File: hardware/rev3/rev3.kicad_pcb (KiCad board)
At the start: 4 copper layers, 55.9 x 76.2 mm, 109 parts, among them J1 USB_B, J2 SMA, J3 CONN_02X09, J4 SMA, J5 CONN_02X09, J6 SMA, J7 SMA, U1 LD1117S33TR, U2 93LCxxB, U3 FT2232H, U4 LTC6409, U5 LTC6269, U6 AD9102, X1 DSC1123, Y1 12MHz

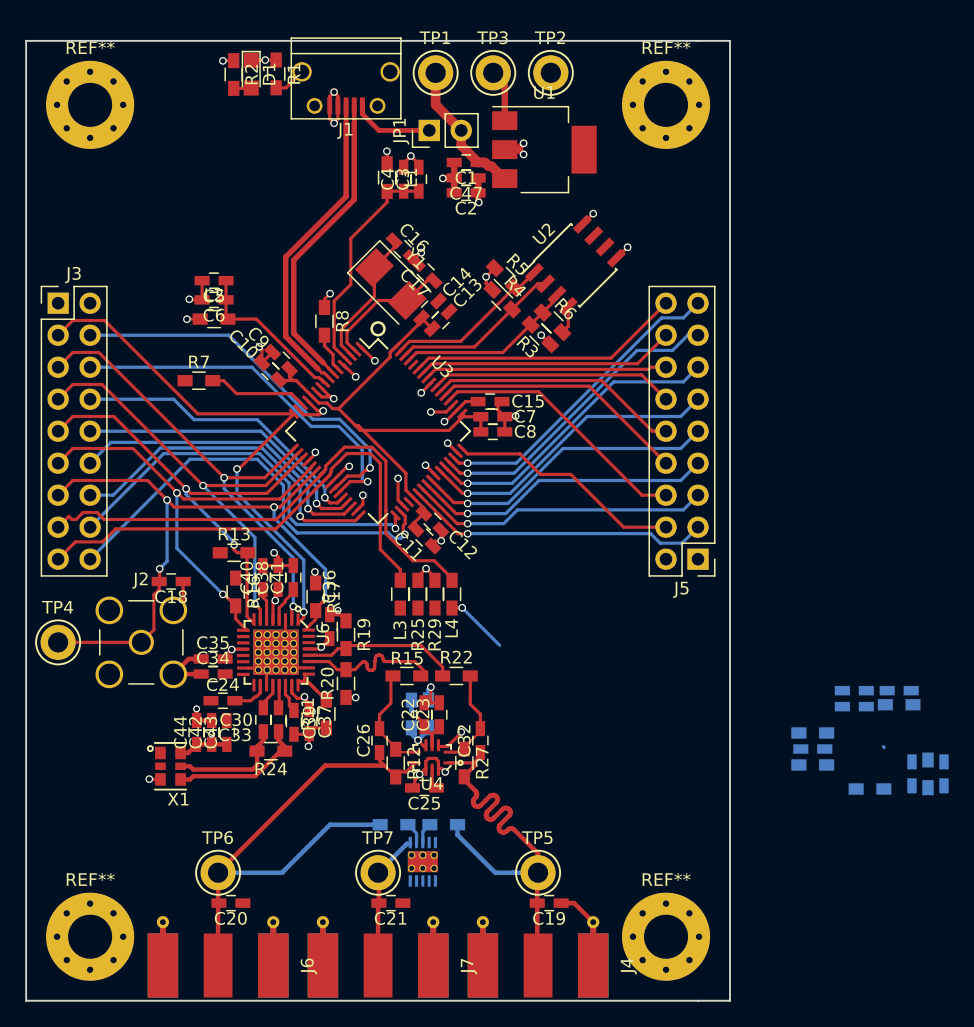
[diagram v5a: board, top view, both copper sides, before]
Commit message: Initial attempt at a complete layout.
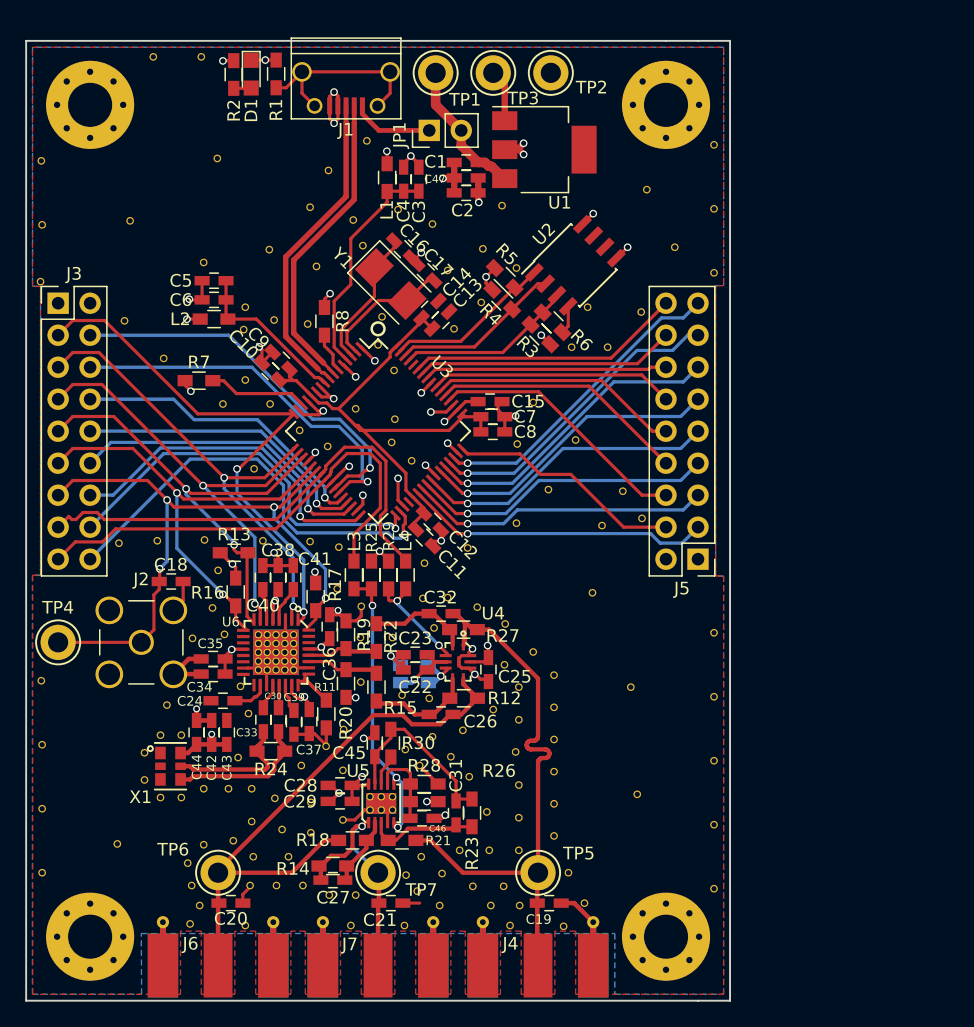
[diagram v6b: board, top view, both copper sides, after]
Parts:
- added ?: , footprints:ManualVia, F.Cu at (133.1, 85.8)
- added ?: , footprints:ManualVia, F.Cu at (141.3, 61.8)
- added ?: , footprints:ManualVia, F.Cu at (160.0, 79.3)
- added ?: , footprints:ManualVia, F.Cu at (162.2, 81.5)
- added ?: , footprints:ManualVia, F.Cu at (163.8, 83.4)
- added ?: , footprints:ManualVia, F.Cu at (163.8, 85.9)
- added ?: , footprints:ManualVia, F.Cu at (163.8, 88.5)
- added ?: , footprints:ManualVia, F.Cu at (163.8, 91.0)
- added ?: , footprints:ManualVia, F.Cu at (163.8, 93.6)
- added ?: , footprints:ManualVia, F.Cu at (163.8, 96.1)
- added ?: , footprints:ManualVia, F.Cu at (165.0, 99.1)
- added ?: , footprints:ManualVia, F.Cu at (166.2, 101.5)
- added ?: , footprints:ManualVia, F.Cu at (137.5, 61.8)
- added ?: , footprints:ManualVia, F.Cu at (164.6, 103.3)
- added ?: , footprints:ManualVia, F.Cu at (160.3, 103.3)
- added ?: , footprints:ManualVia, F.Cu at (161.1, 101.7)
- added ?: , footprints:ManualVia, F.Cu at (158.8, 101.7)
- added ?: , footprints:ManualVia, F.Cu at (154.7, 101.7)
- added ?: , footprints:ManualVia, F.Cu at (153.0, 100.5)
- added ?: , footprints:ManualVia, F.Cu at (152.1, 99.3)
- added ?: , footprints:ManualVia, F.Cu at (153.3, 97.8)
- added ?: , footprints:ManualVia, F.Cu at (154.9, 99.1)
- added ?: , footprints:ManualVia, F.Cu at (157.4, 100.1)
- added ?: , footprints:ManualVia, F.Cu at (130.2, 47.3)
- added ?: , footprints:ManualVia, F.Cu at (159.8, 100.1)
- added ?: , footprints:ManualVia, F.Cu at (135.1, 100.1)
- added ?: , footprints:ManualVia, F.Cu at (134.7, 98.3)
- added ?: , footprints:ManualVia, F.Cu at (136.0, 96.8)
- added ?: , footprints:ManualVia, F.Cu at (138.4, 96.5)
- added ?: , footprints:ManualVia, F.Cu at (139.8, 95.0)
- added ?: , footprints:ManualVia, F.Cu at (141.7, 93.2)
- added ?: , footprints:ManualVia, F.Cu at (148.5, 83.9)
- added ?: , footprints:ManualVia, F.Cu at (147.1, 87.7)
- added ?: , footprints:ManualVia, F.Cu at (145.7, 89.0)
- added ?: , footprints:ManualVia, F.Cu at (137.1, 42.4)
- added ?: , footprints:ManualVia, F.Cu at (143.8, 90.6)
- added ?: , footprints:ManualVia, F.Cu at (139.8, 92.4)
- added ?: , footprints:ManualVia, F.Cu at (138.0, 92.4)
- added ?: , footprints:ManualVia, F.Cu at (136.0, 92.4)
- added ?: , footprints:ManualVia, F.Cu at (134.2, 93.1)
- added ?: , footprints:ManualVia, F.Cu at (161.0, 92.1)
- added ?: , footprints:ManualVia, F.Cu at (161.0, 94.7)
- added ?: , footprints:ManualVia, F.Cu at (161.0, 97.3)
- added ?: , footprints:ManualVia, F.Cu at (158.7, 97.3)
- added ?: , footprints:ManualVia, F.Cu at (156.3, 97.3)
- added ?: , footprints:ManualVia, F.Cu at (158.2, 49.5)
- added ?: , footprints:ManualVia, F.Cu at (158.5, 94.2)
- added ?: , footprints:ManualVia, F.Cu at (157.1, 91.4)
- added ?: , footprints:ManualVia, F.Cu at (154.2, 88.3)
- added ?: , footprints:ManualVia, F.Cu at (156.6, 87.8)
- added ?: , footprints:ManualVia, F.Cu at (155.6, 89.9)
- added ?: , footprints:ManualVia, F.Cu at (153.2, 90.6)
- added ?: , footprints:ManualVia, F.Cu at (152.0, 89.3)
- added ?: , footprints:ManualVia, F.Cu at (161.0, 84.3)
- added ?: , footprints:ManualVia, F.Cu at (161.0, 86.9)
- added ?: , footprints:ManualVia, F.Cu at (159.9, 82.5)
- added ?: , footprints:ManualVia, F.Cu at (173.4, 49.4)
- added ?: , footprints:ManualVia, F.Cu at (159.0, 86.1)
- added ?: , footprints:ManualVia, F.Cu at (160.8, 89.5)
- added ?: , footprints:ManualVia, F.Cu at (148.1, 100.8)
- added ?: , footprints:ManualVia, F.Cu at (146.0, 100.8)
- added ?: , footprints:ManualVia, F.Cu at (143.9, 100.1)
- added ?: , footprints:ManualVia, F.Cu at (141.8, 100.1)
- added ?: , footprints:ManualVia, F.Cu at (139.7, 100.1)
- added ?: , footprints:ManualVia, F.Cu at (132.6, 93.1)
- added ?: , footprints:ManualVia, F.Cu at (131.3, 91.7)
- added ?: , footprints:ManualVia, F.Cu at (131.3, 89.5)
- added ?: , footprints:ManualVia, F.Cu at (171.2, 44.8)
- added ?: , footprints:ManualVia, F.Cu at (132.6, 88.1)
- added ?: , footprints:ManualVia, F.Cu at (134.2, 88.1)
- added ?: , footprints:ManualVia, F.Cu at (154.3, 79.6)
- added ?: , footprints:ManualVia, F.Cu at (151.0, 80.4)
- added ?: , footprints:ManualVia, F.Cu at (151.8, 85.0)
- added ?: , footprints:ManualVia, F.Cu at (153.9, 85.2)
- added ?: , footprints:ManualVia, F.Cu at (147.1, 94.9)
- added ?: , footprints:ManualVia, F.Cu at (144.5, 95.9)
- added ?: , footprints:ManualVia, F.Cu at (142.7, 97.8)
- added ?: , footprints:ManualVia, F.Cu at (144.5, 93.5)
- added ?: , footprints:ManualVia, F.Cu at (159.7, 46.1)
- added ?: , footprints:ManualVia, F.Cu at (142.2, 95.6)
- added ?: , footprints:ManualVia, F.Cu at (140.0, 97.8)
- added ?: , footprints:ManualVia, F.Cu at (147.1, 90.9)
- added ?: , footprints:ManualVia, F.Cu at (154.2, 47.6)
- added ?: , footprints:ManualVia, F.Cu at (155.4, 51.2)
- added ?: , footprints:ManualVia, F.Cu at (138.9, 84.3)
- added ?: , footprints:ManualVia, F.Cu at (149.9, 57.1)
- added ?: , footprints:ManualVia, F.Cu at (150.2, 54.9)
- added ?: , footprints:ManualVia, F.Cu at (160.8, 51.1)
- added ?: , footprints:ManualVia, F.Cu at (155.9, 55.9)
- added ?: , footprints:ManualVia, F.Cu at (158.1, 53.8)
- added ?: , footprints:ManualVia, F.Cu at (151.4, 46.4)
- added ?: , footprints:ManualVia, F.Cu at (148.7, 49.3)
- added ?: , footprints:ManualVia, F.Cu at (145.9, 43.3)
- added ?: , footprints:ManualVia, F.Cu at (144.5, 46.2)
- added ?: , footprints:ManualVia, F.Cu at (176.5, 51.4)
- added ?: , footprints:ManualVia, F.Cu at (144.3, 55.5)
- added ?: , footprints:ManualVia, F.Cu at (176.5, 41.3)
- added ?: , footprints:ManualVia, F.Cu at (176.5, 46.4)
- added ?: , footprints:ManualVia, F.Cu at (132.0, 34.3)
- added ?: , footprints:ManualVia, F.Cu at (135.8, 34.3)
- added ?: , footprints:ManualVia, F.Cu at (123.1, 42.5)
- added ?: , footprints:ManualVia, F.Cu at (123.2, 47.6)
- added ?: , footprints:ManualVia, F.Cu at (123.1, 52.1)
- added ?: , footprints:ManualVia, F.Cu at (139.3, 54.2)
- added ?: , footprints:ManualVia, F.Cu at (141.2, 49.6)
- added ?: , footprints:ManualVia, F.Cu at (141.6, 55.2)
- added ?: , footprints:ManualVia, F.Cu at (139.6, 86.4)
- added ?: , footprints:ManualVia, F.Cu at (136.0, 50.6)
- added ?: , footprints:ManualVia, F.Cu at (129.7, 55.2)
- added ?: , footprints:ManualVia, F.Cu at (139.2, 55.9)
- added ?: , footprints:ManualVia, F.Cu at (132.8, 58.2)
- added ?: , footprints:ManualVia, F.Cu at (139.3, 59.9)
- added ?: , footprints:ManualVia, F.Cu at (140.0, 67.0)
- added ?: , footprints:ManualVia, F.Cu at (145.9, 65.2)
- added ?: , footprints:ManualVia, F.Cu at (143.6, 63.9)
- added ?: , footprints:ManualVia, F.Cu at (151.2, 63.1)
- added ?: , footprints:ManualVia, F.Cu at (151.1, 59.2)
- added ?: , footprints:ManualVia, F.Cu at (138.7, 89.9)
- added ?: , footprints:ManualVia, F.Cu at (148.1, 62.2)
- added ?: , footprints:ManualVia, F.Cu at (152.5, 66.4)
- added ?: , footprints:ManualVia, F.Cu at (150.9, 64.9)
- added ?: , footprints:ManualVia, F.Cu at (169.9, 84.3)
- added ?: , footprints:ManualVia, F.Cu at (170.4, 92.8)
- added ?: , footprints:ManualVia, F.Cu at (166.9, 76.8)
- added ?: , footprints:ManualVia, F.Cu at (167.6, 71.5)
- added ?: , footprints:ManualVia, F.Cu at (163.4, 68.6)
- added ?: , footprints:ManualVia, F.Cu at (160.8, 71.3)
- added ?: , footprints:ManualVia, F.Cu at (157.0, 73.3)
- added ?: , footprints:ManualVia, F.Cu at (145.0, 50.9)
- added ?: , footprints:ManualVia, F.Cu at (153.5, 74.5)
- added ?: , footprints:ManualVia, F.Cu at (170.8, 54.5)
- added ?: , footprints:ManualVia, F.Cu at (166.5, 54.2)
- added ?: , footprints:ManualVia, F.Cu at (168.1, 57.3)
- added ?: , footprints:ManualVia, F.Cu at (165.2, 57.3)
- added ?: , footprints:ManualVia, F.Cu at (160.9, 65.0)
- added ?: , footprints:ManualVia, F.Cu at (162.2, 61.7)
- added ?: , footprints:ManualVia, F.Cu at (165.5, 64.7)
- added ?: , footprints:ManualVia, F.Cu at (169.3, 68.8)
- added ?: , footprints:ManualVia, F.Cu at (170.8, 70.9)
- added ?: , footprints:ManualVia, F.Cu at (147.9, 47.2)
- added ?: , footprints:ManualVia, F.Cu at (176.5, 80.0)
- added ?: , footprints:ManualVia, F.Cu at (176.5, 85.1)
- added ?: , footprints:ManualVia, F.Cu at (176.5, 95.2)
- added ?: , footprints:ManualVia, F.Cu at (176.5, 100.3)
- added ?: , footprints:ManualVia, F.Cu at (176.5, 90.2)
- added ?: , footprints:ManualVia, F.Cu at (123.1, 83.8)
- added ?: , footprints:ManualVia, F.Cu at (123.2, 88.9)
- added ?: , footprints:ManualVia, F.Cu at (123.2, 94.0)
- added ?: , footprints:ManualVia, F.Cu at (123.2, 99.1)
- added ?: , footprints:ManualVia, F.Cu at (135.7, 101.7)
- added ?: , footprints:ManualVia, F.Cu at (149.0, 41.0)
- added ?: , footprints:ManualVia, F.Cu at (134.9, 103.1)
- added ?: , footprints:ManualVia, F.Cu at (139.3, 103.3)
- added ?: , footprints:ManualVia, F.Cu at (147.7, 103.3)
- added ?: , footprints:ManualVia, F.Cu at (152.0, 103.3)
- added ?: , footprints:ManualVia, F.Cu at (135.1, 80.5)
- added ?: , footprints:ManualVia, F.Cu at (136.7, 78.0)
- added ?: , footprints:ManualVia, F.Cu at (137.7, 80.1)
- added ?: , footprints:ManualVia, F.Cu at (129.3, 72.9)
- added ?: , footprints:ManualVia, F.Cu at (132.3, 72.7)
- added ?: , footprints:ManualVia, F.Cu at (137.2, 75.1)
- added ?: , footprints:ManualVia, F.Cu at (129.2, 96.8)
- added ?: , footprints:ManualVia, F.Cu at (136.1, 72.6)
- added ?: , footprints:ManualVia, F.Cu at (140.7, 72.7)
- added ?: , footprints:ManualVia, F.Cu at (144.5, 72.8)
- added ?: , footprints:ManualVia, F.Cu at (146.7, 73.2)
- added ?: , footprints:ManualVia, F.Cu at (146.6, 76.5)
- added ?: , footprints:ManualVia, F.Cu at (148.5, 77.9)
- added ?: , footprints:ManualVia, F.Cu at (148.5, 80.4)
- added ?: , footprints:ManualVia, F.Cu at (153.4, 77.3)
- added ?: , footprints:ManualVia, F.Cu at (155.4, 77.2)
- added ?: , footprints:ManualVia, F.Cu at (157.7, 78.0)
-  C19: renamed from C19
- C27, C28, C29, C31, C45, C46, R14, R18, R21, R23, R26, R28, R30, U5: moved to F.Cu
- moved C27 47.4 mm to (146.3, 99.6)
- moved R14 46.7 mm to (146.3, 98.5)
- moved C45 45.2 mm to (149.6, 88.9)
- moved C28 41.5 mm to (146.8, 92.1), turned to 180 degrees
- moved C29 41.5 mm to (146.8, 93.4), turned to 180 degrees
- moved R30 38.2 mm to (150.9, 88.8), turned to 90 degrees
- moved C31 36.3 mm to (156.0, 94.3), turned to 270 degrees
- moved R23 36.3 mm to (157.3, 94.3), turned to 90 degrees
- moved C46 31.5 mm to (153.3, 94.7), turned to 0 degrees
- moved R28 31.1 mm to (153.5, 92.0), turned to 0 degrees
- moved R26 31.0 mm to (153.5, 93.4), turned to 180 degrees
- moved C25 10.7 mm to (158.6, 82.9), turned to 270 degrees
- moved R27 10.6 mm to (156.6, 79.8), turned to 0 degrees
- moved C32 10.5 mm to (154.9, 78.5), turned to 180 degrees
- moved U4 7.87 mm to (156.2, 82.3), turned to 270 degrees
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- renumbered REF** to ?
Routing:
- net GNDA: track 88.0 -> 143.6 mm, vias 30 -> 31
- net Net-(L3-Pad1): track 0.00 -> 22.6 mm, vias 0 -> 3
- net /Analog/+1.65V: track 0.00 -> 14.7 mm
- net Net-(J1-Pad5): track 2.57 -> 15.8 mm
- net +3V3: track 43.7 -> 55.1 mm, vias 21 -> 26
- net VOUT: track 10.9 -> 19.8 mm, vias 0 -> 1
- net Net-(C31-Pad2): track 1.74 -> 9.12 mm
- net VOUT+: track 41.5 -> 47.9 mm
- net Net-(C46-Pad1): track 0.00 -> 6.44 mm
- net Net-(R19-Pad2): track 12.7 -> 6.33 mm
- net Net-(R15-Pad1): track 12.8 -> 6.59 mm
- net VOUT-: track 43.1 -> 47.6 mm
- net Net-(C27-Pad1): track 1.80 -> 6.18 mm
- net AMP0_EN: track 42.7 -> 39.0 mm
- net Net-(C26-Pad2): track 8.51 -> 10.8 mm
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- added copper zone on B.Cu, net GNDA
- added copper zone on F.Cu, net GNDA
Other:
- net class 100ohm_diff: clearance 0.1905 -> 0.18796

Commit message: Final touches.
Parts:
- removed the ? at (173.4, 49.4)
- removed the ? at (176.5, 51.4)
- removed the ? at (176.5, 41.3)
- removed the ? at (176.5, 46.4)
- added ?: , footprints:ManualVia, F.Cu at (156.2, 103.1)
- added ?: , footprints:ManualVia, F.Cu at (173.4, 52.1)
- added ?: , footprints:ManualVia, F.Cu at (158.2, 41.1)
- added ?: , footprints:ManualVia, F.Cu at (154.2, 34.3)
- added ?: , footprints:ManualVia, F.Cu at (159.4, 34.3)
- added ?: , footprints:ManualVia, F.Cu at (164.5, 34.3)
- added ?: , footprints:ManualVia, F.Cu at (168.9, 34.3)
- added ?: , footprints:ManualVia, F.Cu at (163.3, 43.4)
- added ?: , footprints:ManualVia, F.Cu at (168.3, 43.6)
- added ?: , footprints:ManualVia, F.Cu at (142.6, 38.7)
- added ?: , footprints:ManualVia, F.Cu at (143.5, 103.1)
- added G***: LOGO, footprints:oshw, F.Cu at (136.1, 46.0)
- moved TP1 25.7 mm to (175.3, 50.5)
- moved ? 19.9 mm to (152.3, 38.7)
- moved TP3 19.8 mm to (175.3, 46.9)
- moved TP2 14.0 mm to (175.3, 43.2)
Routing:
- net Net-(C1-Pad1): track 11.2 -> 23.8 mm
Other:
- net class 100ish_ohm: via_drill 0.4064 -> 0.3048
- net class 100ohm_diff: via_drill 0.4064 -> 0.3048
- net class 50ohm: via_drill 0.4064 -> 0.3048
- net class Default: via_drill 0.4064 -> 0.3048
- rule via_min_drill: 0.3556 -> 0.3048
- board text added: "+3.3V"
- board text added: "GND"
- board text added: "TRIGGER"
- board text added: "VBUS"
- board text added: "VO+"
- board text added: "VO-"
- board text added: "VOUT"
- board text added: "Wavegen Rev. 3"

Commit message: Move OSHW logo. Add github link.
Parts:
- moved G*** 54.2 mm to (168.0, 89.8), turned to 90 degrees
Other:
- board text added: "github.com:Fifty-Nine/wavegen"
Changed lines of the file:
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@@
     (links 544)
     (no_connects 0)
-    (area 115.150714 30.41 184.569286 119.656001)
+    (area 121.844999 32.944999 177.875001 109.295001)
     (thickness 1.6)
-    (drawings 16)
+    (drawings 17)
     (tracks 1019)
     (zones 0)
@@
   )
   (module footprints:oshw (layer F.Cu)
-    (at 136.144 45.974)
-    (fp_text reference G*** (at 0 0) (layer F.SilkS) hide
+    (at 168.021 89.789 90)
+    (fp_text reference G*** (at 0 0 90) (layer F.SilkS) hide
       (effects (font (thickness 0.3)))
     )
-    (fp_text value LOGO (at 0.75 0) (layer F.SilkS) hide
+    (fp_text value LOGO (at 0.75 0 90) (layer F.SilkS) hide
       (effects (font (thickness 0.3)))
     )
@@
       (net 41 GNDA) (zone_connect 2))
   )
+  (gr_text github.com:Fifty-Nine/wavegen (at 175.387 90.17 90) (layer F.SilkS)
+    (effects (font (size 0.762 0.762) (thickness 0.1)))
+  )
   (gr_text VBUS (at 171.45 50.546) (layer F.SilkS)
     (effects (font (size 1.016 1.016) (thickness 0.127)))
@@
     (effects (font (size 1.016 1.016) (thickness 0.127)))
   )
-  (gr_text "Wavegen Rev. 3" (at 135.943987 40.132) (layer F.SilkS)
-    (effects (font (size 0.762 0.762) (thickness 0.127)))
+  (gr_text "Wavegen Rev. 3" (at 174.117 89.789 90) (layer F.SilkS)
+    (effects (font (size 0.762 0.762) (thickness 0.1)))
   )
   (gr_text TRIGGER (at 127.7366 86.2076) (layer F.SilkS)
